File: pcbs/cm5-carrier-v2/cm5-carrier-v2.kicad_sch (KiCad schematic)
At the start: 11 parts

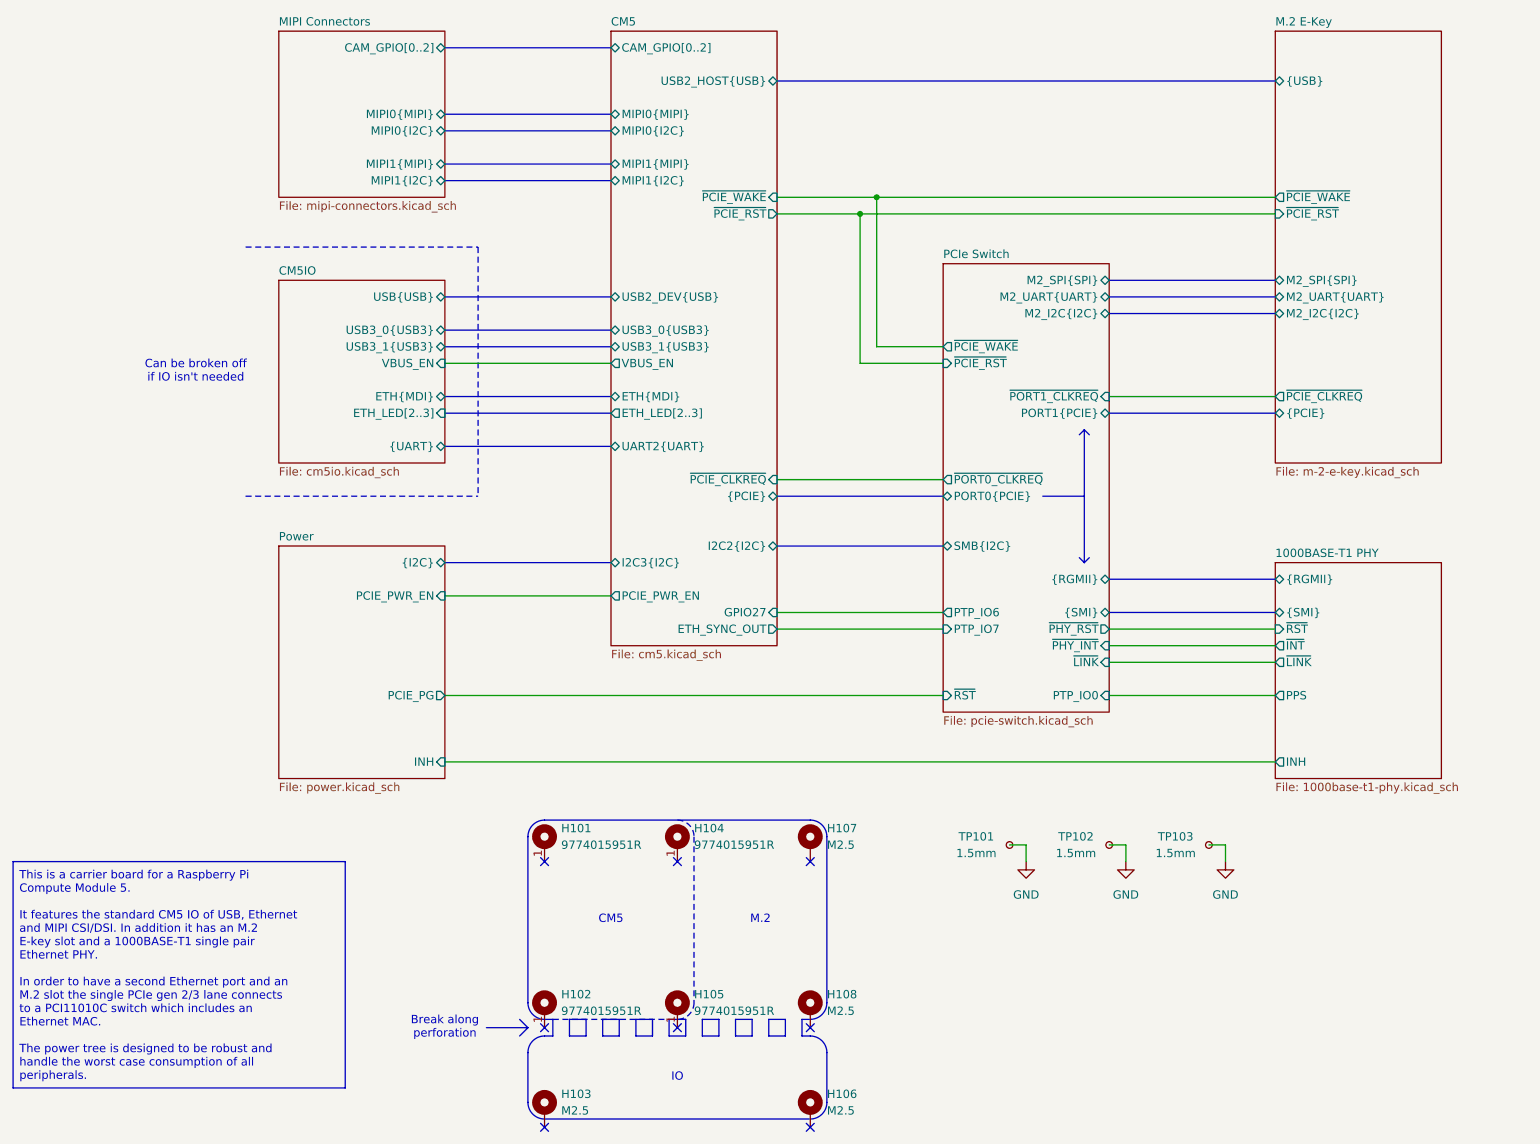
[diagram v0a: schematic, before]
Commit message: Changed UART connector to I2C
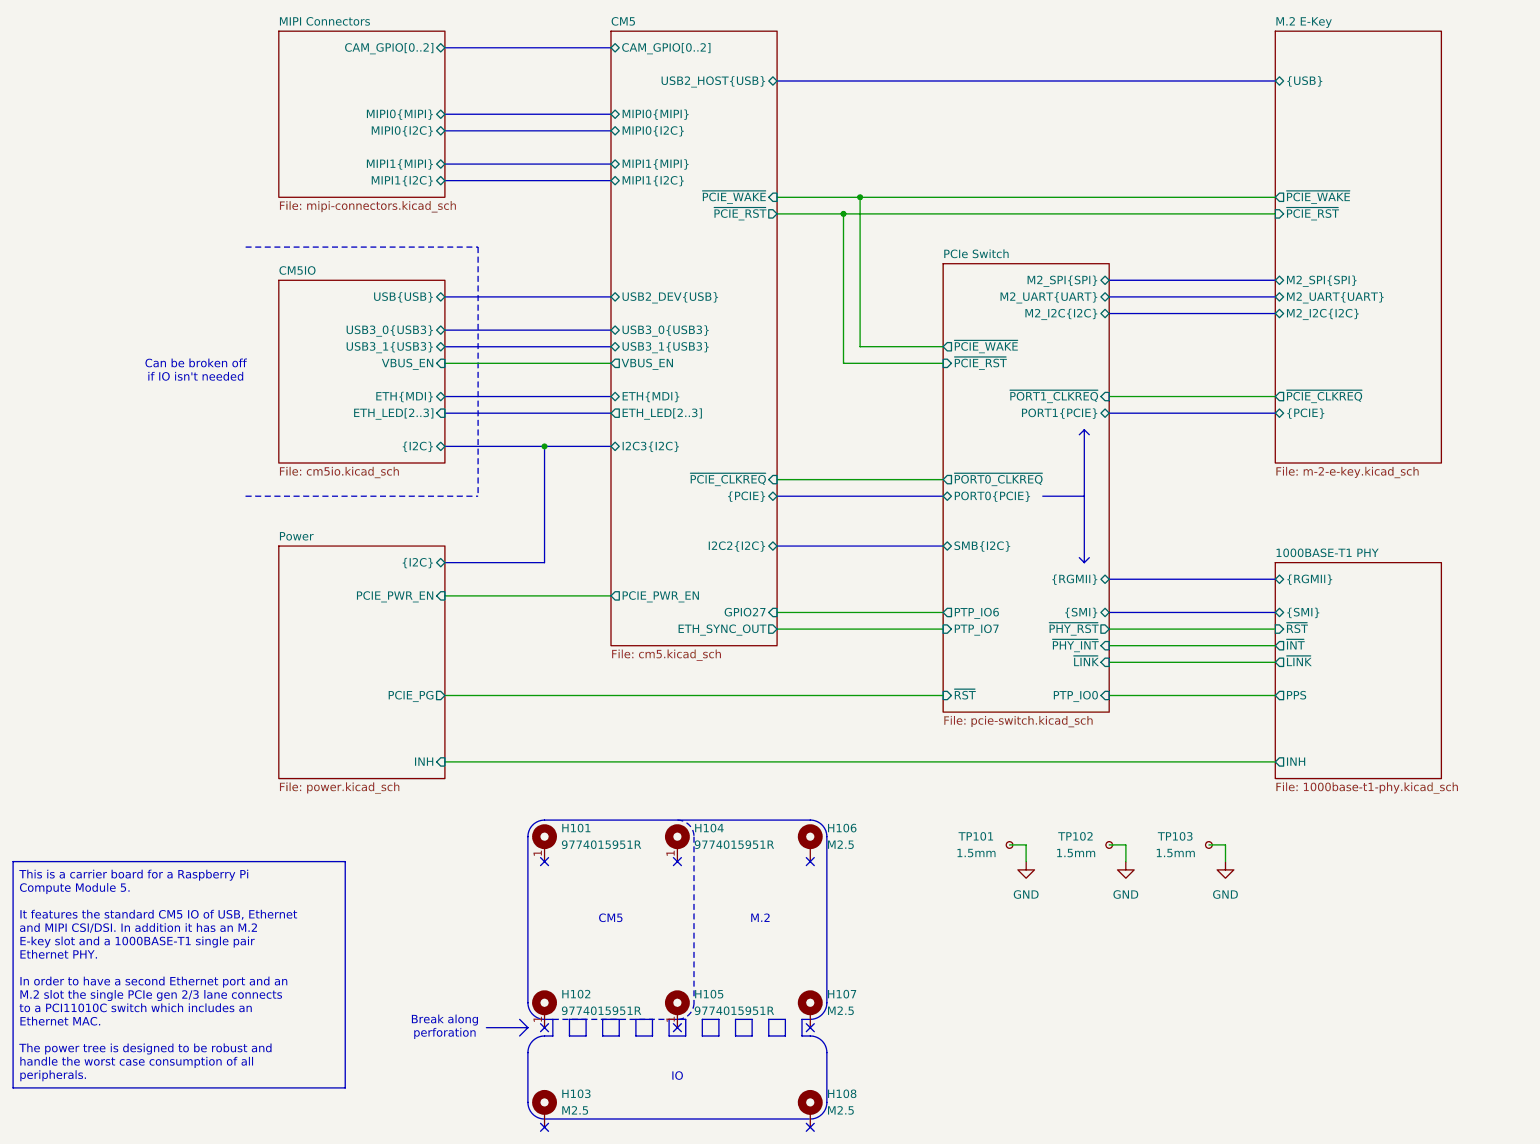
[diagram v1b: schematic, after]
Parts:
- renumbered H107 to H106, H108 to H107, H106 to H108
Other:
- sheet CM5 ports: added none; removed UART2{UART}
- sheet CM5IO ports: added {I2C}; removed {UART}
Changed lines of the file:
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@@
 	)
 	(junction
-		(at 160.02 53.34)
+		(at 111.76 88.9)
 		(diameter 0)
 		(color 0 0 0 0)
 	)
 	(junction
-		(at 162.56 50.8)
+		(at 160.02 50.8)
+		(diameter 0)
+		(color 0 0 0 0)
+	)
+	(junction
+		(at 157.48 53.34)
 		(diameter 0)
 		(color 0 0 0 0)
@@
 	(bus
 		(pts
-			(xy 147.32 33.02) (xy 223.52 33.02)
+			(xy 96.52 88.9) (xy 111.76 88.9)
 		)
 		(stroke
@@
 		)
 	)
-	(wire
+	(bus
 		(pts
-			(xy 147.32 116.84) (xy 172.72 116.84)
+			(xy 147.32 33.02) (xy 223.52 33.02)
 		)
 		(stroke
@@
 		)
 	)
-	(polyline
+	(wire
 		(pts
-			(xy 115.57 176.53) (xy 115.57 179.07)
+			(xy 147.32 116.84) (xy 172.72 116.84)
 		)
 		(stroke
@@
 		)
 	)
-	(bus
+	(polyline
 		(pts
-			(xy 96.52 66.04) (xy 121.92 66.04)
+			(xy 115.57 176.53) (xy 115.57 179.07)
 		)
 		(stroke
@@
 		)
 	)
-	(wire
+	(bus
 		(pts
-			(xy 162.56 50.8) (xy 223.52 50.8)
+			(xy 96.52 66.04) (xy 121.92 66.04)
 		)
 		(stroke
@@
 	(wire
 		(pts
-			(xy 172.72 73.66) (xy 162.56 73.66)
+			(xy 172.72 73.66) (xy 160.02 73.66)
 		)
 		(stroke
@@
 	(bus
 		(pts
-			(xy 96.52 106.68) (xy 121.92 106.68)
+			(xy 96.52 106.68) (xy 111.76 106.68)
 		)
 		(stroke
@@
 	(wire
 		(pts
-			(xy 160.02 53.34) (xy 223.52 53.34)
-		)
-		(stroke
-			(width 0)
-			(type default)
-		)
-	)
-	(wire
-		(pts
-			(xy 162.56 50.8) (xy 162.56 73.66)
+			(xy 160.02 50.8) (xy 160.02 73.66)
 		)
 		(stroke
@@
 	(wire
 		(pts
-			(xy 147.32 50.8) (xy 162.56 50.8)
+			(xy 147.32 50.8) (xy 160.02 50.8)
 		)
 		(stroke
@@
 	(wire
 		(pts
-			(xy 160.02 53.34) (xy 160.02 76.2)
+			(xy 157.48 53.34) (xy 157.48 76.2)
 		)
 		(stroke
@@
 		)
 	)
+	(bus
+		(pts
+			(xy 111.76 88.9) (xy 121.92 88.9)
+		)
+		(stroke
+			(width 0)
+			(type default)
+		)
+	)
 	(wire
 		(pts
@@
 	(wire
 		(pts
-			(xy 172.72 76.2) (xy 160.02 76.2)
+			(xy 172.72 76.2) (xy 157.48 76.2)
 		)
 		(stroke
@@
 		)
 	)
+	(wire
+		(pts
+			(xy 160.02 50.8) (xy 223.52 50.8)
+		)
+		(stroke
+			(width 0)
+			(type default)
+		)
+	)
 	(bus
 		(pts
@@
 		)
 	)
-	(bus
-		(pts
-			(xy 96.52 88.9) (xy 121.92 88.9)
-		)
-		(stroke
-			(width 0)
-			(type default)
-		)
-	)
 	(polyline
 		(pts
@@
 		)
 	)
+	(bus
+		(pts
+			(xy 111.76 88.9) (xy 111.76 106.68)
+		)
+		(stroke
+			(width 0)
+			(type default)
+		)
+	)
 	(polyline
 		(pts
@@
 	(wire
 		(pts
-			(xy 147.32 53.34) (xy 160.02 53.34)
+			(xy 147.32 53.34) (xy 157.48 53.34)
 		)
 		(stroke
@@
 	(wire
 		(pts
+			(xy 157.48 53.34) (xy 223.52 53.34)
+		)
+		(stroke
+			(width 0)
+			(type default)
+		)
+	)
+	(wire
+		(pts
 			(xy 198.12 149.86) (xy 200.66 149.86)
 		)
@@
 		(dnp no)
 		(fields_autoplaced yes)
-		(property "Reference" "H107"
+		(property "Reference" "H106"
 			(at 154.94 147.3199 0)
 			(show_name no)
@@
 			(project "cm5-carrier-v2"
 				(path "/f91ec272-d09a-4038-bbbb-962739a92c51"
-					(reference "H107")
+					(reference "H106")
 					(unit 1)
 				)
@@
 		(dnp no)
 		(fields_autoplaced yes)
-		(property "Reference" "H106"
+		(property "Reference" "H108"
 			(at 154.94 187.9599 0)
 			(show_name no)
@@
 			(project "cm5-carrier-v2"
 				(path "/f91ec272-d09a-4038-bbbb-962739a92c51"
-					(reference "H106")
+					(reference "H108")
 					(unit 1)
 				)
@@
 		(dnp no)
 		(fields_autoplaced yes)
-		(property "Reference" "H108"
+		(property "Reference" "H107"
 			(at 154.94 172.7199 0)
 			(show_name no)
@@
 			(project "cm5-carrier-v2"
 				(path "/f91ec272-d09a-4038-bbbb-962739a92c51"
-					(reference "H108")
+					(reference "H107")
 					(unit 1)
 				)
@@
 		)
 		(pin "I2C3{I2C}" bidirectional
-			(at 121.92 106.68 180)
-			(effects
-				(font
-					(size 1.27 1.27)
-				)
-				(justify left)
-			)
-		)
-		(pin "UART2{UART}" bidirectional
 			(at 121.92 88.9 180)
 			(effects
@@
 			)
 		)
-		(pin "{UART}" bidirectional
+		(pin "{I2C}" bidirectional
 			(at 96.52 88.9 0)
 			(effects
